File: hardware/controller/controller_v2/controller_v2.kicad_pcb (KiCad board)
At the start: 2 copper layers, 48.5 x 38.5 mm, 22 parts, among them J1 USB_C_Receptacle_USB2.0_16P, J2 Conn_01x04_Socket, SW1 SW_Push, SW2 SW_Push, U1 ESP32-C3-MINI-1-N4, U2 74AHCT1G125, U4 AMS1117-3.3

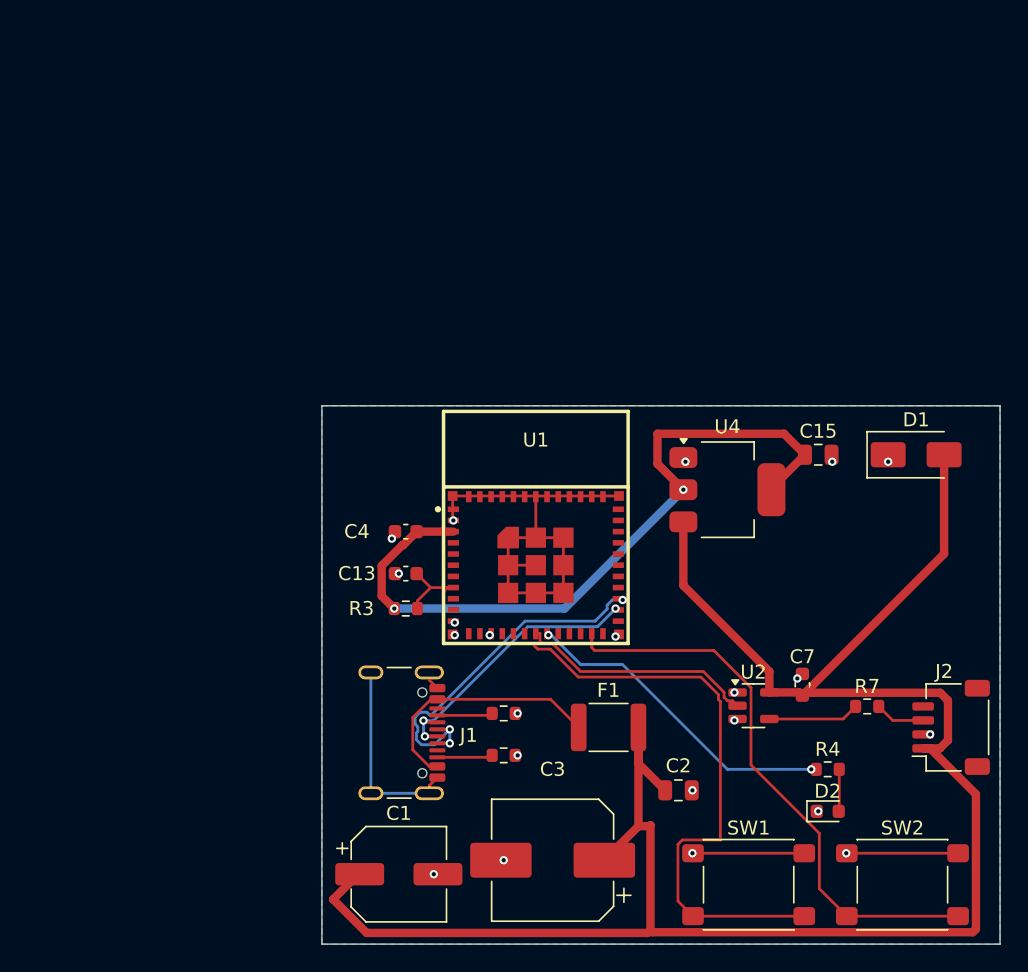
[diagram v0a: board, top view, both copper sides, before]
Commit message: Add octave-module flex PCB (fab-ready) + hardware to main
octave-module: uniform 13.708 mm LED pitch (caps aligned), solder lap-seam (J2 output / J3 input pads) with J2 plated 0.8 mm solder-access holes, full routing + GND pour, J1 placement; seam-lap footprint library; spacing/seam design docs; regenerated BOM + production files (J1 DNP, caps C14663, LEDs C2761795). Also controller_v2 + hardware BOM/docs.

Co-Authored-By: Claude Opus 4.8 <noreply@anthropic.com>
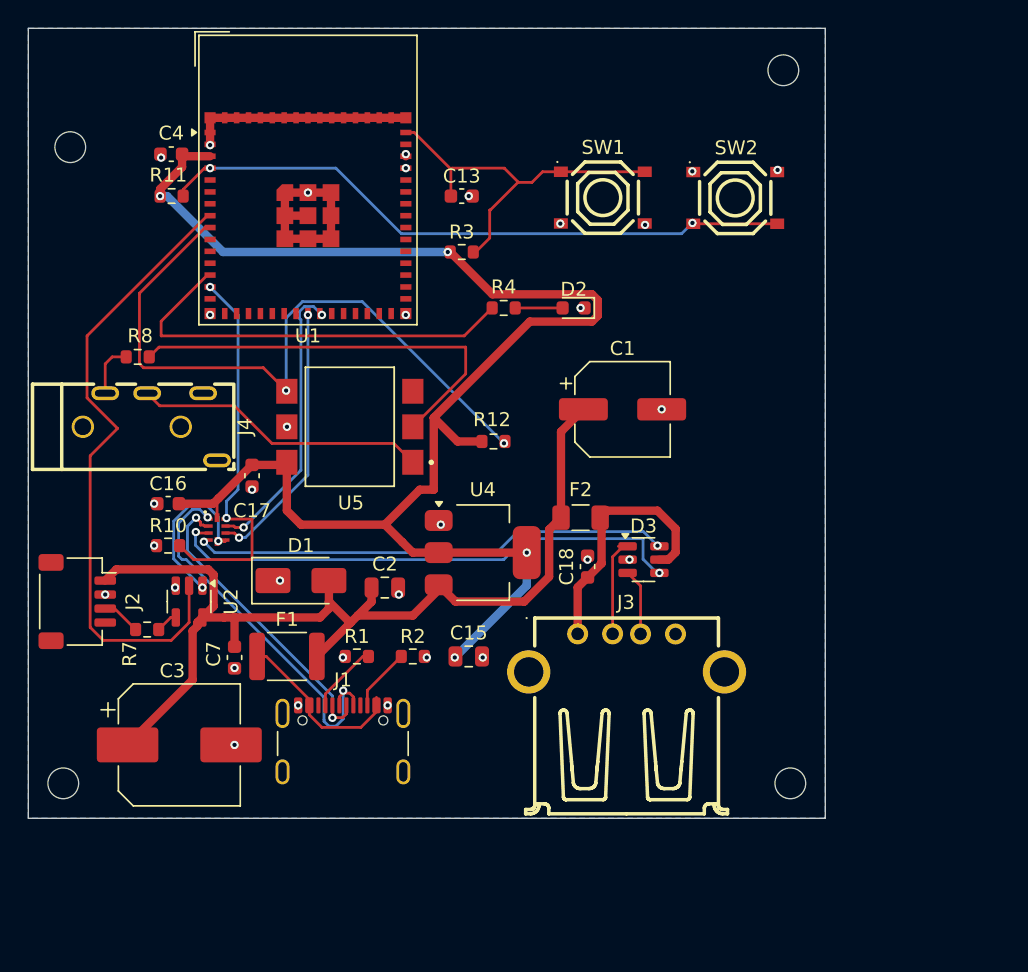
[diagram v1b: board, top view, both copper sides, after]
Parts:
- added C16: 0.1uF, Capacitor_SMD:C_0603_1608Metric, F.Cu at (110.0, 89.0)
- added C17: 0.1uF, Capacitor_SMD:C_0603_1608Metric, F.Cu at (116.0, 87.0)
- added C18: 0.1uF, Capacitor_SMD:C_0603_1608Metric, F.Cu at (140.0, 93.5)
- added D3: USBLC6-2SC6, Package_TO_SOT_SMD:SOT-23-6, F.Cu at (144.0, 93.0)
- added F2: 500mA, Fuse:Fuse_1206_3216Metric, F.Cu at (139.5, 90.0)
- added J3: USB_A, easyeda2kicad:USB-A-TH__USB-AF-90, F.Cu at (142.8, 99.7)
- added J4: PJ-320A, easyeda2kicad:AUDIO-TH_XKB_PJ-320A, F.Cu at (109.5, 83.5)
- added R10: 10k, Resistor_SMD:R_0603_1608Metric, F.Cu at (110.0, 92.0)
- added R11: 10k, Resistor_SMD:R_0603_1608Metric, F.Cu at (110.2, 67.0)
- added R12: 1k, Resistor_SMD:R_0603_1608Metric, F.Cu at (133.3, 84.5)
- added R8: 220, Resistor_SMD:R_0603_1608Metric, F.Cu at (107.8, 78.5)
- added REF**: MountingHole_2.2mm_M2, MountingHole:MountingHole_2.2mm_M2, F.Cu at (103.0, 63.5)
- added REF**: MountingHole_2.2mm_M2, MountingHole:MountingHole_2.2mm_M2, F.Cu at (154.0, 58.0)
- added REF**: MountingHole_2.2mm_M2, MountingHole:MountingHole_2.2mm_M2, F.Cu at (154.5, 109.0)
- added REF**: MountingHole_2.2mm_M2, MountingHole:MountingHole_2.2mm_M2, F.Cu at (102.5, 109.0)
- added U3: TS3USB221A, TS3USB221A:QFN-10-RSE, F.Cu at (113.5, 90.8)
- added U5: H11L1, H11L1SM:IC_H11L1SM, F.Cu at (123.0, 83.5)
- SW1, SW2: footprint Button_Switch_SMD:SW_SPST_PTS645Sx43SMTR92 -> easyeda2kicad:SW-SMD_4P-L5.1-W5.1-P3.70-LS6.5-TL_H1.5
- U1: value ESP32-C3-MINI-1-N4 -> ESP32-S3-MINI-1; footprint ESP32-C3-MINI-1:WIFIM-SMD_ESP32-C3-MINI-1 -> RF_Module:ESP32-S2-MINI-1
- moved J2 63.1 mm to (103.5, 96.0), turned to -90 degrees
- moved R7 51.8 mm to (108.5, 98.0), turned to 180 degrees
- moved SW2 50.6 mm to (150.6, 67.1)
- moved SW1 50.2 mm to (141.1, 67.1)
- moved D1 44.9 mm to (119.5, 94.5)
- moved U2 41.0 mm to (111.5, 96.0), turned to -90 degrees
- moved C7 40.7 mm to (114.8, 100.0), turned to -90 degrees
- moved D2 40.3 mm to (139.0, 75.0), turned to 180 degrees
- moved R4 40.3 mm to (134.0, 75.0)
- moved C1 36.9 mm to (142.5, 82.2)
- moved U1 32.0 mm to (120.0, 65.8)
- moved C4 31.8 mm to (110.2, 64.0)
- moved C15 28.9 mm to (131.5, 99.9)
- moved C3 27.9 mm to (110.8, 106.2), turned to 0 degrees
- moved C13 27.3 mm to (131.0, 67.0), turned to 0 degrees
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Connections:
- C13 pad 1: Net-(U1-EN) -> /EN
- J1 pad A6: /D_P -> /USBC_DP
- J1 pad A7: /D_N -> /USBC_DM
- J1 pad B6: /D_P -> /USBC_DP
- J1 pad B7: /D_N -> /USBC_DM
- R3 pad 1: Net-(U1-EN) -> +3.3V
- R3 pad 2: +3.3V -> /EN
- R4 pad 1: Net-(U1-IO5) -> /STATUS
- SW1 pad 1: GND -> /EN
- SW1 pad 2: Net-(U1-EN) -> GND
- SW2 pad 2: Net-(U1-IO9) -> /BOOT
- U1 pad 11: GND -> unconnected-(U1-IO7-Pad11)
- U1 pad 13: unconnected-(U1-IO1-Pad13) -> /STATUS
- U1 pad 14: GND -> /USB_SEL
- U1 pad 18: /LED_DATA_3V3 -> unconnected-(U1-IO14-Pad18)
- U1 pad 19: Net-(U1-IO5) -> unconnected-(U1-IO15-Pad19)
- U1 pad 23: Net-(U1-IO9) -> /USB_DM
- U1 pad 24: unconnected-(U1-NC-Pad24) -> /USB_DP
- U1 pad 26: /D_N -> unconnected-(U1-IO26-Pad26)
- U1 pad 27: /D_P -> unconnected-(U1-IO47-Pad27)
- U1 pad 36: GND -> unconnected-(U1-IO40-Pad36)
- U1 pad 37: GND -> unconnected-(U1-IO41-Pad37)
- U1 pad 38: GND -> unconnected-(U1-IO42-Pad38)
- U1 pad 39: GND -> unconnected-(U1-TXD0-Pad39)
- U1 pad 4: unconnected-(U1-NC-Pad4) -> /BOOT
- U1 pad 40: GND -> unconnected-(U1-RXD0-Pad40)
- U1 pad 41: GND -> unconnected-(U1-IO45-Pad41)
- U1 pad 44: GND -> unconnected-(U1-IO46-Pad44)
- U1 pad 45: GND -> /EN
- U1 pad 8: Net-(U1-EN) -> /LED_DATA_3V3
- U1 pad 9: unconnected-(U1-NC-Pad9) -> /MIDI_RX
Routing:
- net +5V: track 143.0 -> 74.1 mm
- net +3.3V: track 53.2 -> 111.8 mm, vias 2 -> 4
- net Net-(U1-EN): track 57.9 -> 0.00 mm
- net /MIDI_RX: track 0.00 -> 49.0 mm, vias 0 -> 2
- net /BOOT: track 0.00 -> 46.0 mm, vias 0 -> 2
- net Net-(U1-IO9): track 40.7 -> 0.00 mm
- net /USBA_DP: track 0.00 -> 38.0 mm, vias 0 -> 2
- net /USBA_DM: track 0.00 -> 34.4 mm, vias 0 -> 2
- net /STATUS: track 0.00 -> 30.4 mm
- net Net-(R8-Pad2): track 0.00 -> 30.2 mm
- net /LED_DATA_3V3: track 17.2 -> 45.5 mm
- net /USB_SEL: track 0.00 -> 28.2 mm, vias 0 -> 2
- net /USBC_DP: track 0.00 -> 27.9 mm, vias 0 -> 2
- net /EN: track 0.00 -> 27.3 mm
- net /D_P: track 26.5 -> 0.00 mm, vias 3 -> 0
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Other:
- board size 48.5 x 38.5 mm -> 57 x 56.5 mm
